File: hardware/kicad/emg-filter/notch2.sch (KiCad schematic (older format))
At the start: 72 parts, among them U28 LM4565, U29 LM4565, U30 LM4565, U31 LM4565, U32 LM4565, U33 LM4565, U34 LM4565, U35 LM4565

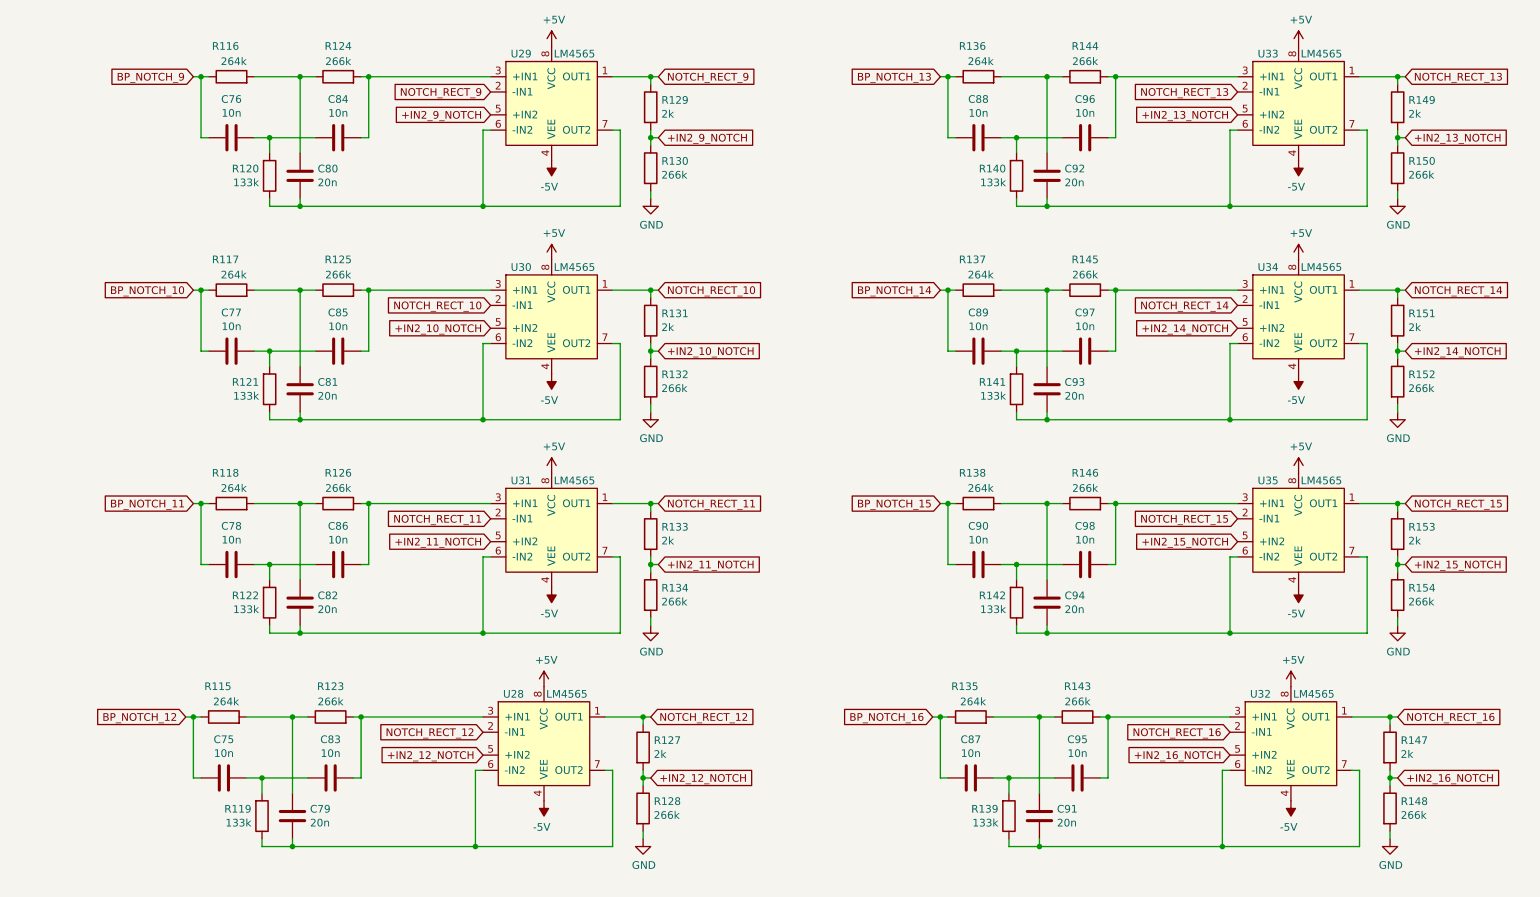
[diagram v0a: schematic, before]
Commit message: pi connector and adc
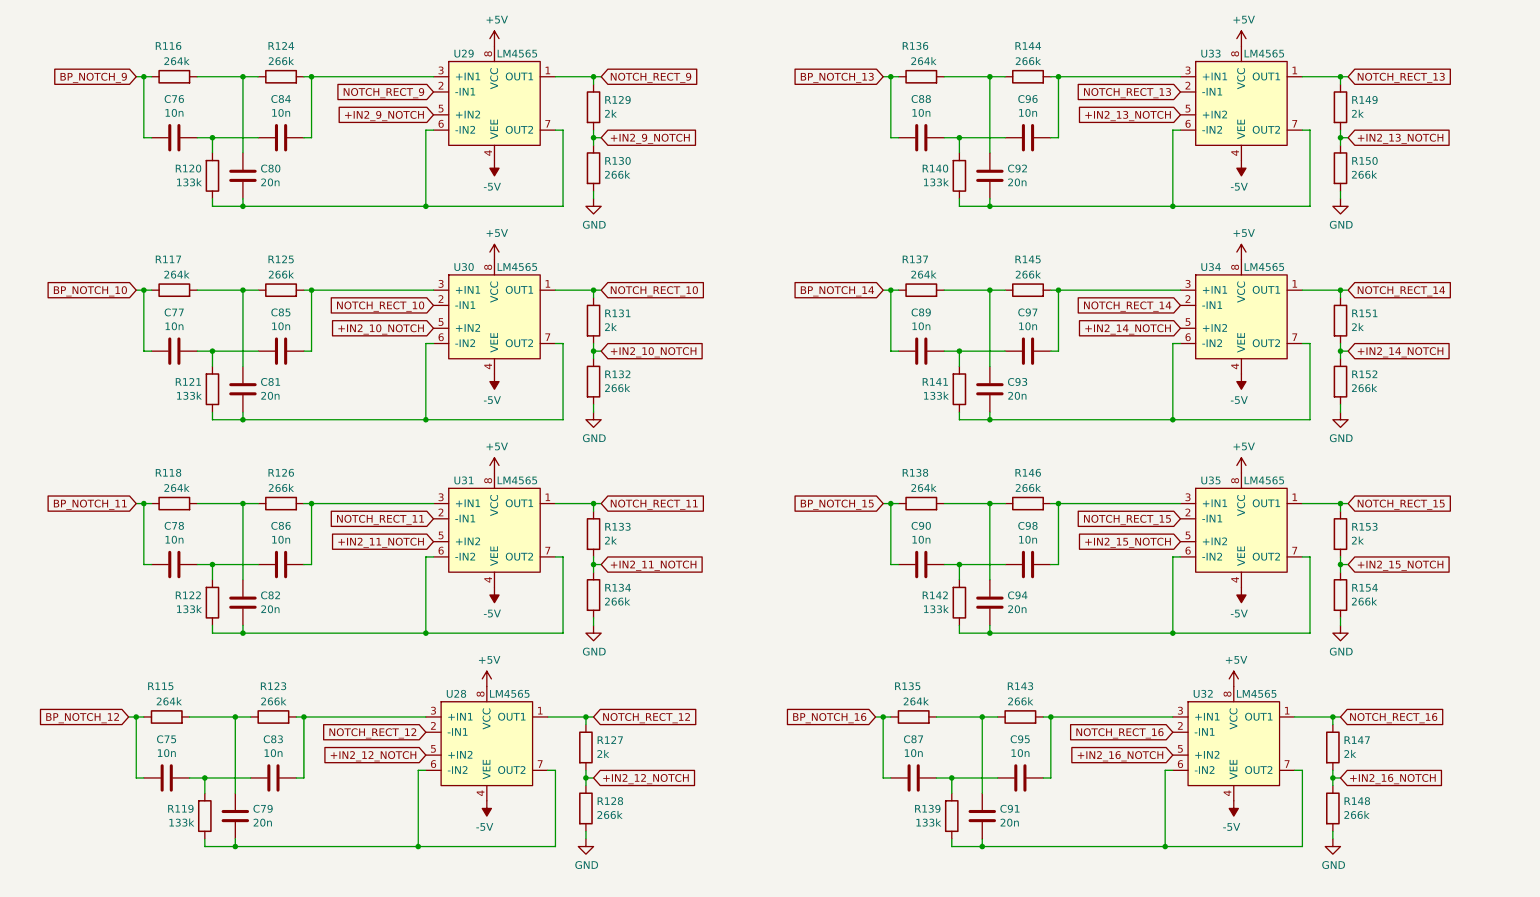
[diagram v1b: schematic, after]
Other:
- moved on the sheet: C75, C76, C77, C78, C79, C80, C81, C82, C83, C84, C85, C86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

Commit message: fixed rect labels
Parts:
- renumbered C75 to C150, C76 to C151, C77 to C152, C78 to C153, C79 to C154, C80 to C155, C81 to C156, C82 to C157, C83 to C158, C84 to C159, C85 to C160, C86 to C161, C87 to C162, C88 to C163, C89 to C164, C90 to C165, C91 to C166, C92 to C167, C93 to C168, C94 to C169, C95 to C170, C96 to C171, C97 to C172, C98 to C173, R115 to R112, R116 to R113, R117 to R114, R118 to R115, R119 to R116, R120 to R117, R121 to R118, R122 to R119, R123 to R120, R124 to R121, R125 to R122, R126 to R123, R127 to R124, R128 to R125, R129 to R126, R130 to R127, R131 to R128, R132 to R129, R133 to R130, R134 to R131, R135 to R132, R136 to R133, R137 to R134, R138 to R135, R139 to R136, R140 to R137, R141 to R138, R142 to R139, R143 to R140, R144 to R141, R145 to R142, R146 to R143, R147 to R144, R148 to R145, R149 to R146, R150 to R147, R151 to R148, R152 to R149, R153 to R150, R154 to R151, U28 to U27, U29 to U28, U30 to U29, U31 to U30, U32 to U31, U33 to U32, U34 to U33, U35 to U34

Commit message: footprint association
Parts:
- C150, C151, C152, C153, C154, C155, C156, C157, C158, C159, C160, C161, C162, C163, C164, C165, C166, C167, C168, C169, C170, C171, C172, C173: footprint (none) -> Capacitor_SMD:C_0805_2012Metric
- R100: renamed from R132; footprint (none) -> Resistor_SMD:R_0805_2012Metric
- R101: renamed from R133; footprint (none) -> Resistor_SMD:R_0805_2012Metric
- R102: renamed from R134; footprint (none) -> Resistor_SMD:R_0805_2012Metric
- R103: renamed from R135; footprint (none) -> Resistor_SMD:R_0805_2012Metric
- R104: renamed from R136; footprint (none) -> Resistor_SMD:R_0805_2012Metric
- R105: renamed from R137; footprint (none) -> Resistor_SMD:R_0805_2012Metric
- R106: renamed from R138; footprint (none) -> Resistor_SMD:R_0805_2012Metric
- R107: renamed from R139; footprint (none) -> Resistor_SMD:R_0805_2012Metric
- R108: renamed from R140; footprint (none) -> Resistor_SMD:R_0805_2012Metric
- R109: renamed from R141; footprint (none) -> Resistor_SMD:R_0805_2012Metric
- R110: renamed from R142; footprint (none) -> Resistor_SMD:R_0805_2012Metric
- R111: renamed from R143; footprint (none) -> Resistor_SMD:R_0805_2012Metric
- R112: renamed from R144; footprint (none) -> Resistor_SMD:R_0805_2012Metric
- R113: renamed from R145; footprint (none) -> Resistor_SMD:R_0805_2012Metric
- R114: renamed from R146; footprint (none) -> Resistor_SMD:R_0805_2012Metric
- R115: renamed from R147; footprint (none) -> Resistor_SMD:R_0805_2012Metric
- R116: renamed from R148; footprint (none) -> Resistor_SMD:R_0805_2012Metric
- R117: renamed from R149; footprint (none) -> Resistor_SMD:R_0805_2012Metric
- R118: renamed from R150; footprint (none) -> Resistor_SMD:R_0805_2012Metric
- R119: renamed from R151; footprint (none) -> Resistor_SMD:R_0805_2012Metric
- R80: renamed from R112; footprint (none) -> Resistor_SMD:R_0805_2012Metric
- R81: renamed from R113; footprint (none) -> Resistor_SMD:R_0805_2012Metric
- R82: renamed from R114; footprint (none) -> Resistor_SMD:R_0805_2012Metric
- R83: renamed from R115; footprint (none) -> Resistor_SMD:R_0805_2012Metric
- R84: renamed from R116; footprint (none) -> Resistor_SMD:R_0805_2012Metric
- R85: renamed from R117; footprint (none) -> Resistor_SMD:R_0805_2012Metric
- R86: renamed from R118; footprint (none) -> Resistor_SMD:R_0805_2012Metric
- R87: renamed from R119; footprint (none) -> Resistor_SMD:R_0805_2012Metric
- R88: renamed from R120; footprint (none) -> Resistor_SMD:R_0805_2012Metric
- R89: renamed from R121; footprint (none) -> Resistor_SMD:R_0805_2012Metric
- R90: renamed from R122; footprint (none) -> Resistor_SMD:R_0805_2012Metric
- R91: renamed from R123; footprint (none) -> Resistor_SMD:R_0805_2012Metric
- R92: renamed from R124; footprint (none) -> Resistor_SMD:R_0805_2012Metric
- R93: renamed from R125; footprint (none) -> Resistor_SMD:R_0805_2012Metric
- R94: renamed from R126; footprint (none) -> Resistor_SMD:R_0805_2012Metric
- R95: renamed from R127; footprint (none) -> Resistor_SMD:R_0805_2012Metric
- R96: renamed from R128; footprint (none) -> Resistor_SMD:R_0805_2012Metric
- R97: renamed from R129; footprint (none) -> Resistor_SMD:R_0805_2012Metric
- R98: renamed from R130; footprint (none) -> Resistor_SMD:R_0805_2012Metric
- R99: renamed from R131; footprint (none) -> Resistor_SMD:R_0805_2012Metric
- renumbered U27 to U19, U28 to U20, U29 to U21, U30 to U22, U31 to U23, U32 to U24, U33 to U25, U34 to U26

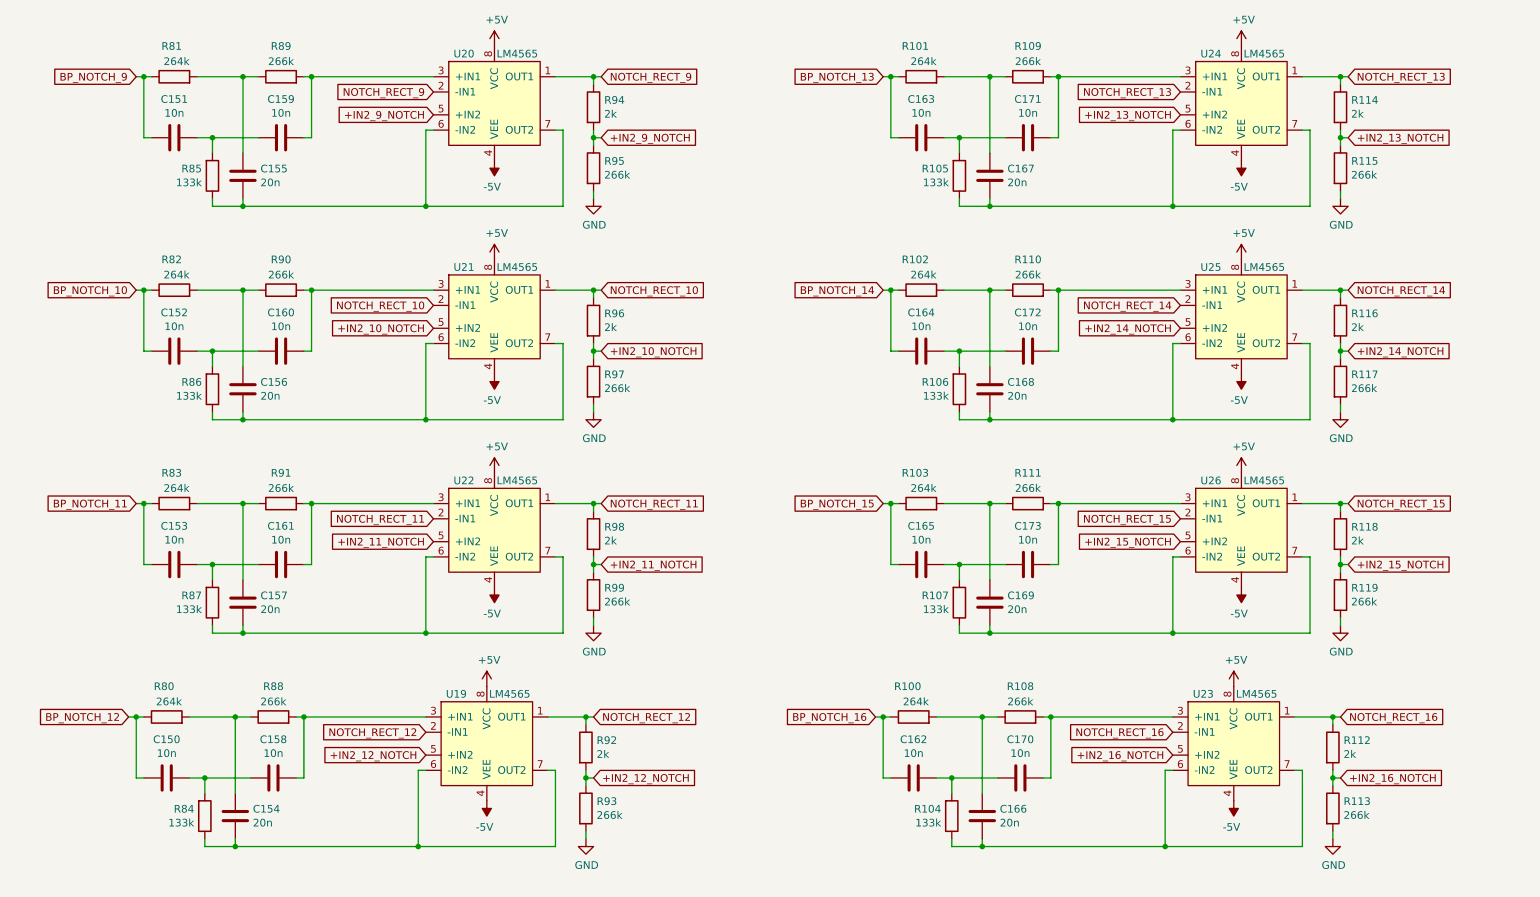
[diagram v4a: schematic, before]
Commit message: slip 264k and 266k, now 2x132k and 2x133k
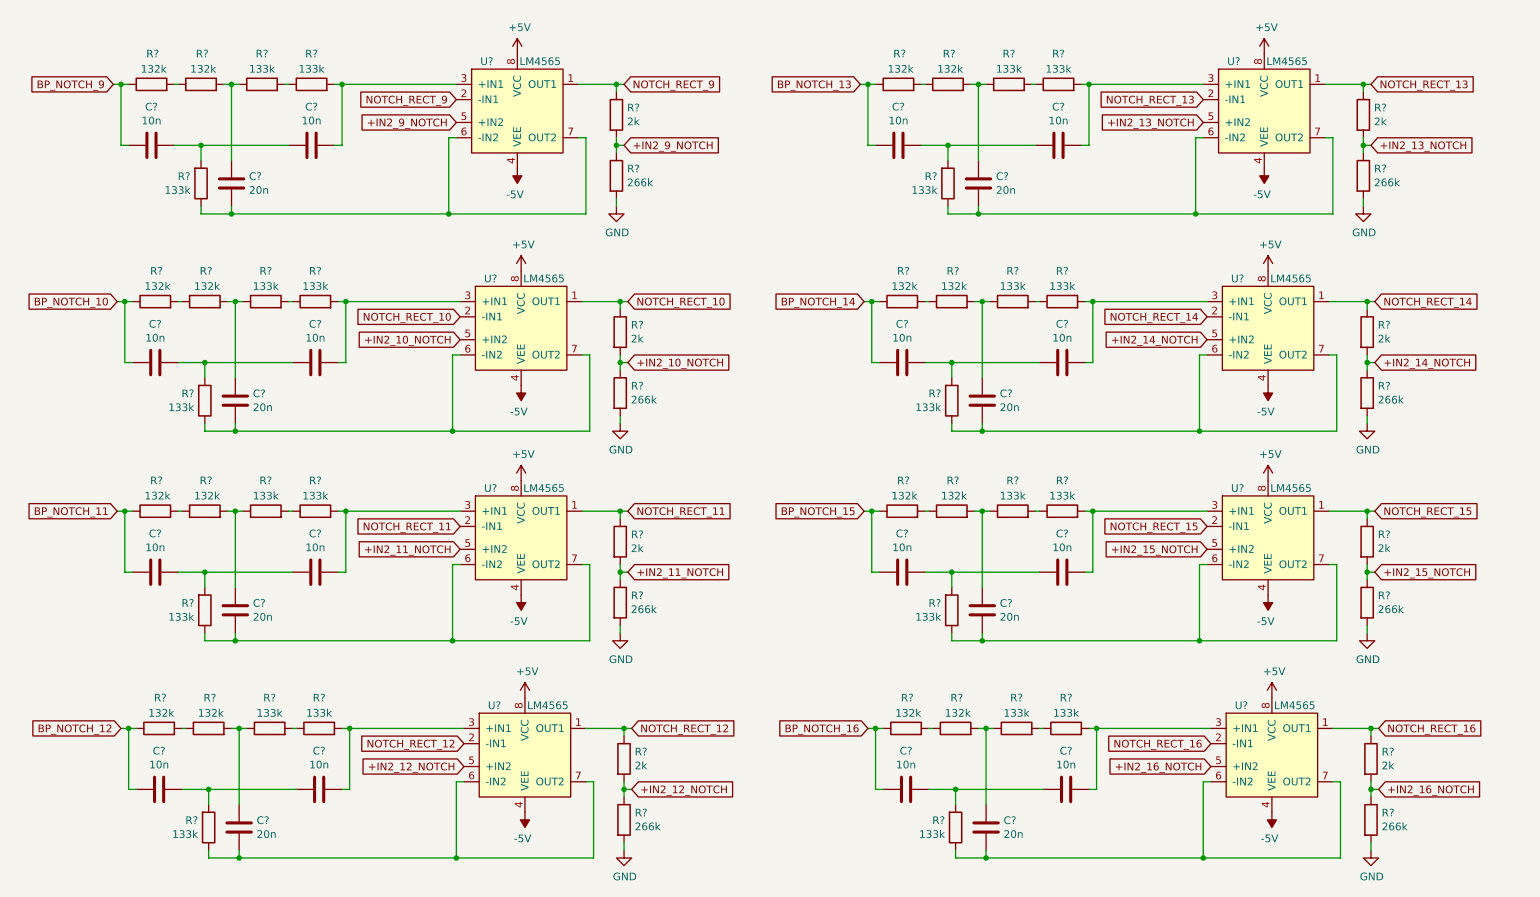
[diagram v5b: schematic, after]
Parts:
- removed C150, C151, C152, C153, C158, C159, C160, C161, C162, C163, C164, C165, C170, C171, C172, C173: 10n, Capacitor_SMD:C_0805_2012Metric, symbol Device:C
- removed C154, C155, C156, C157, C166, C167, C168, C169: 20n, Capacitor_SMD:C_0805_2012Metric, symbol Device:C
- removed R100, R101, R102, R103, R80, R81, R82, R83: 264k, Resistor_SMD:R_0805_2012Metric, symbol Device:R
- removed R104, R105, R106, R107, R84, R85, R86, R87: 133k, Resistor_SMD:R_0805_2012Metric, symbol Device:R
- removed R108, R109, R110, R111, R113, R115, R117, R119, R88, R89, R90, R91, R93, R95, R97, R99: 266k, Resistor_SMD:R_0805_2012Metric, symbol Device:R
- removed R112, R114, R116, R118, R92, R94, R96, R98: 2k, Resistor_SMD:R_0805_2012Metric, symbol Device:R
- removed U19, U20, U21, U22, U23, U24, U25, U26: LM4565, symbol emg-filter:LM4565
- added C? (x8): 20n, Capacitor_SMD:C_0805_2012Metric, symbol Device:C
- added C? (x16): 10n, Capacitor_SMD:C_0805_2012Metric, symbol Device:C
- added R? (x24): 133k, Resistor_SMD:R_0805_2012Metric, symbol Device:R
- added R? (x8): 2k, Resistor_SMD:R_0805_2012Metric, symbol Device:R
- added R? (x8): 266k, Resistor_SMD:R_0805_2012Metric, symbol Device:R
- added R? (x16): 132k, Resistor_SMD:R_0805_2012Metric, symbol Device:R
- added U? (x8): LM4565, symbol emg-filter:LM4565
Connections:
- net +5V: now also U?.8 (VCC), U?.8 (VCC), U?.8 (VCC), U?.8 (VCC), U?.8 (VCC), U?.8 (VCC), U?.8 (VCC), U?.8 (VCC)
- net +IN2_10_NOTCH: now also R?.1, R?.2, U?.5 (+IN2)
- net +IN2_11_NOTCH: now also R?.1, R?.2, U?.5 (+IN2)
- net +IN2_12_NOTCH: now also R?.1, R?.2, U?.5 (+IN2)
- net +IN2_13_NOTCH: now also R?.1, R?.2, U?.5 (+IN2)
- net +IN2_14_NOTCH: now also R?.1, R?.2, U?.5 (+IN2)
- net +IN2_15_NOTCH: now also R?.1, R?.2, U?.5 (+IN2)
- net +IN2_16_NOTCH: now also R?.1, R?.2, U?.5 (+IN2)
- net +IN2_9_NOTCH: now also R?.1, R?.2, U?.5 (+IN2)
- net -5V: now also U?.4 (VEE), U?.4 (VEE), U?.4 (VEE), U?.4 (VEE), U?.4 (VEE), U?.4 (VEE), U?.4 (VEE), U?.4 (VEE)
- net BP_NOTCH_10: now also C?.2, R?.1
- net BP_NOTCH_11: now also C?.2, R?.1
- net BP_NOTCH_12: now also C?.2, R?.1
- net BP_NOTCH_13: now also C?.2, R?.1
- net BP_NOTCH_14: now also C?.2, R?.1
- net BP_NOTCH_15: now also C?.2, R?.1
- net BP_NOTCH_16: now also C?.2, R?.1
- net BP_NOTCH_9: now also C?.2, R?.1
- net GND: now also R?.2, R?.2, R?.2, R?.2, R?.2, R?.2, R?.2, R?.2
- net NOTCH_RECT_10: now also R?.1, U?.1 (OUT1), U?.2 (-IN1)
- net NOTCH_RECT_11: now also R?.1, U?.1 (OUT1), U?.2 (-IN1)
- net NOTCH_RECT_12: now also R?.1, U?.1 (OUT1), U?.2 (-IN1)
- net NOTCH_RECT_13: now also R?.1, U?.1 (OUT1), U?.2 (-IN1)
- net NOTCH_RECT_14: now also R?.1, U?.1 (OUT1), U?.2 (-IN1)
- net NOTCH_RECT_15: now also R?.1, U?.1 (OUT1), U?.2 (-IN1)
- net NOTCH_RECT_16: now also R?.1, U?.1 (OUT1), U?.2 (-IN1)
- net NOTCH_RECT_9: now also R?.1, U?.1 (OUT1), U?.2 (-IN1)
- new net: C?.1, R?.2, U?.3 (+IN1) (x8)
- new net: C?.1, R?.1, U?.6 (-IN2), U?.7 (OUT2) (x8)
- new net: R?.1, R?.2 (x16)
- new net: C?.1, C?.2, R?.2 (x8)
- new net: C?.2, R?.1, R?.2 (x8)

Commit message: Solving Stuff for Free
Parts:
- gave numbers to parts that had none: 88

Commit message: pcb
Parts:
- U19, U20, U21, U22, U23, U24, U25, U26: footprint (none) -> emg-filter:LM4565
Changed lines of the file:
@@
 F 0 "U19" H 3825 1500 50  0000 C CNN
 F 1 "LM4565" H 4175 1500 50  0000 C CNN
-F 2 "" H 5025 1200 50  0001 C CNN
+F 2 "emg-filter:LM4565" H 5025 1200 50  0001 C CNN
 F 3 "" H 5025 1200 50  0001 C CNN
 	1    4025 1200
@@
 F 0 "U20" H 3850 2925 50  0000 C CNN
 F 1 "LM4565" H 4200 2925 50  0000 C CNN
-F 2 "" H 5050 2625 50  0001 C CNN
+F 2 "emg-filter:LM4565" H 5050 2625 50  0001 C CNN
 F 3 "" H 5050 2625 50  0001 C CNN
 	1    4050 2625
@@
 F 0 "U21" H 3850 4300 50  0000 C CNN
 F 1 "LM4565" H 4200 4300 50  0000 C CNN
-F 2 "" H 5050 4000 50  0001 C CNN
+F 2 "emg-filter:LM4565" H 5050 4000 50  0001 C CNN
 F 3 "" H 5050 4000 50  0001 C CNN
 	1    4050 4000
@@
 F 0 "U22" H 3875 5725 50  0000 C CNN
 F 1 "LM4565" H 4225 5725 50  0000 C CNN
-F 2 "" H 5075 5425 50  0001 C CNN
+F 2 "emg-filter:LM4565" H 5075 5425 50  0001 C CNN
 F 3 "" H 5075 5425 50  0001 C CNN
 	1    4075 5425
@@
 F 0 "U23" H 8725 1500 50  0000 C CNN
 F 1 "LM4565" H 9075 1500 50  0000 C CNN
-F 2 "" H 9925 1200 50  0001 C CNN
+F 2 "emg-filter:LM4565" H 9925 1200 50  0001 C CNN
 F 3 "" H 9925 1200 50  0001 C CNN
 	1    8925 1200
@@
 F 0 "U24" H 8750 2925 50  0000 C CNN
 F 1 "LM4565" H 9100 2925 50  0000 C CNN
-F 2 "" H 9950 2625 50  0001 C CNN
+F 2 "emg-filter:LM4565" H 9950 2625 50  0001 C CNN
 F 3 "" H 9950 2625 50  0001 C CNN
 	1    8950 2625
@@
 F 0 "U25" H 8750 4300 50  0000 C CNN
 F 1 "LM4565" H 9100 4300 50  0000 C CNN
-F 2 "" H 9950 4000 50  0001 C CNN
+F 2 "emg-filter:LM4565" H 9950 4000 50  0001 C CNN
 F 3 "" H 9950 4000 50  0001 C CNN
 	1    8950 4000
@@
 F 0 "U26" H 8775 5725 50  0000 C CNN
 F 1 "LM4565" H 9125 5725 50  0000 C CNN
-F 2 "" H 9975 5425 50  0001 C CNN
+F 2 "emg-filter:LM4565" H 9975 5425 50  0001 C CNN
 F 3 "" H 9975 5425 50  0001 C CNN
 	1    8975 5425
